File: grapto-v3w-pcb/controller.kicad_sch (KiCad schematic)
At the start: 34 parts, among them J5 Conn_01x06_Female, J6 USB_C_Receptacle_USB2.0, J7 USB_C_Receptacle_USB2.0, J8 Conn_01x06_Male, U11 USBLC6-4SC6, U12 ACN52840, U13 TPS2110, U14 LM3676SD-3.3

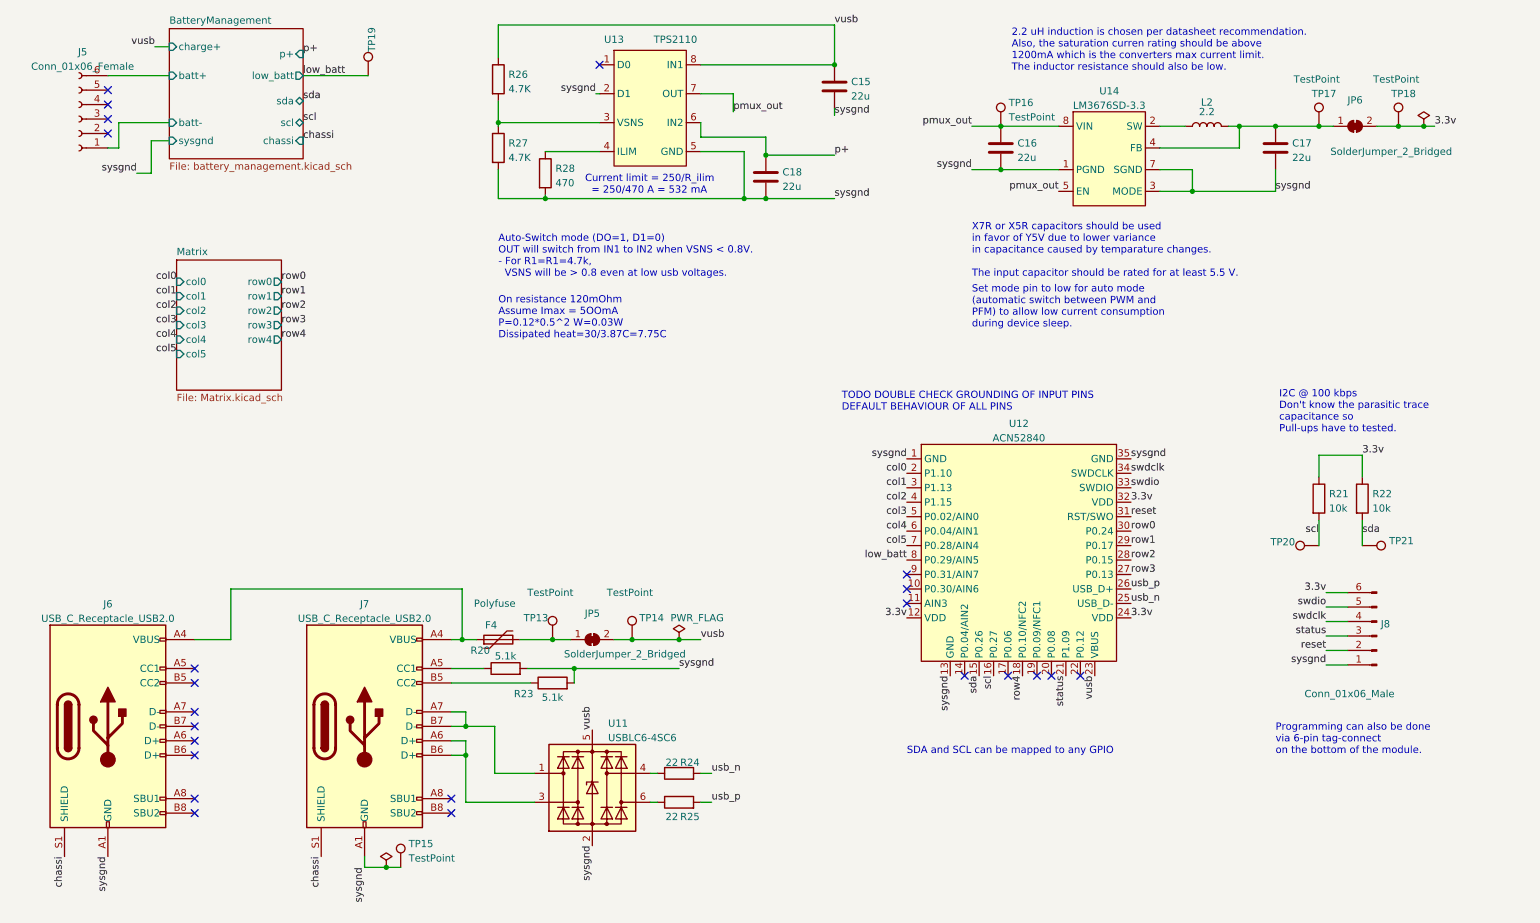
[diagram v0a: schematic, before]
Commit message: More layout. esd chip problems.
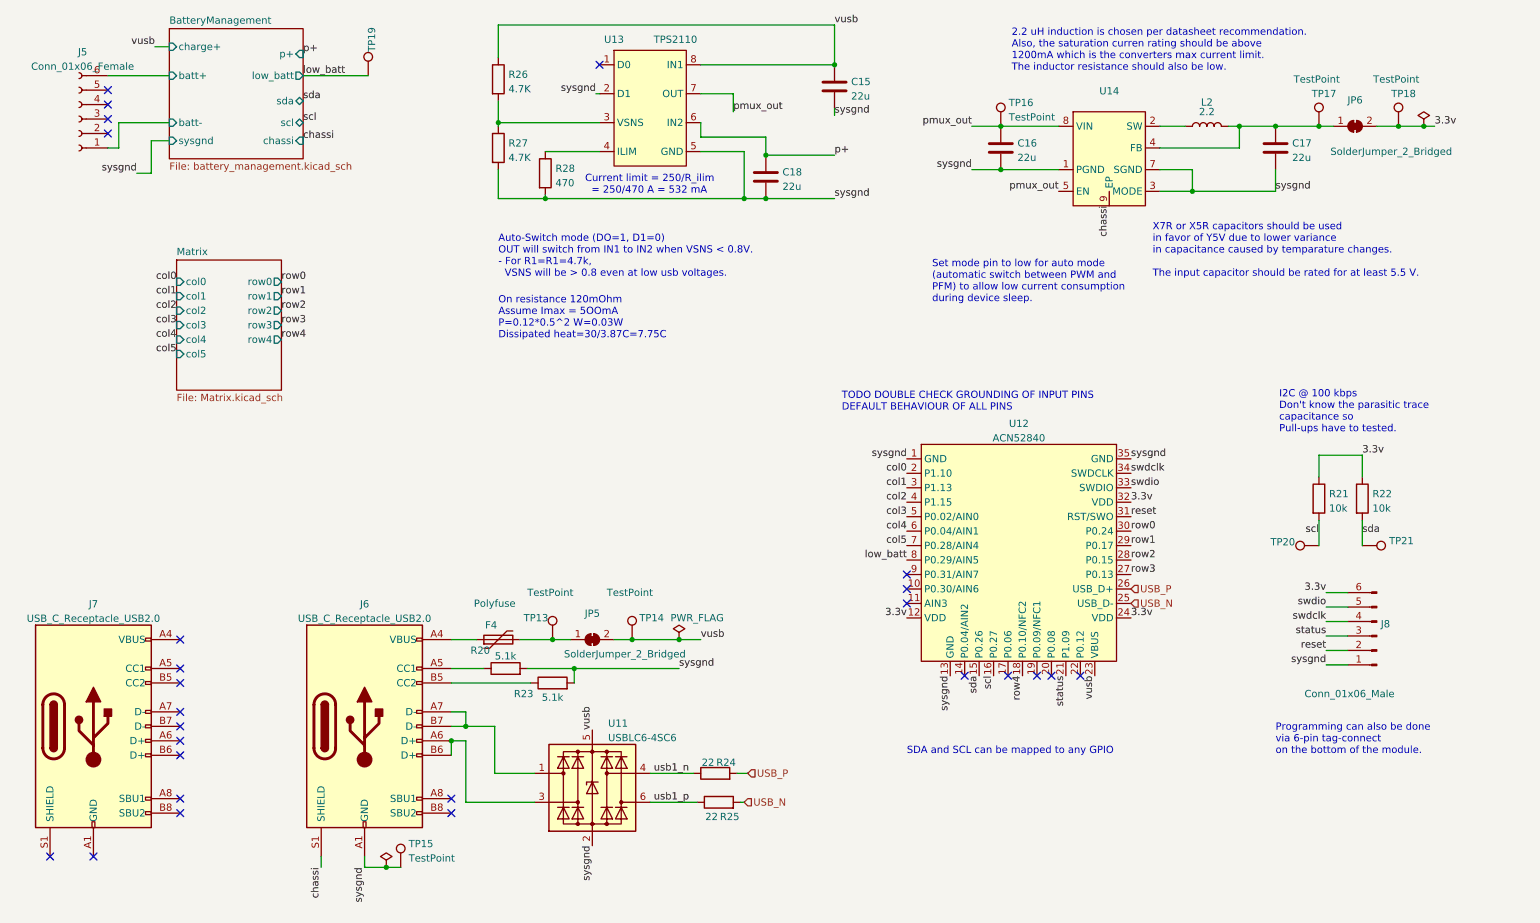
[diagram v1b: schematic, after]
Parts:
- U14: value LM3676SD-3.3 -> (none); footprint Package_SON:WSON-8-1EP_3x3mm_P0.5mm_EP1.6x2.0mm -> (none)
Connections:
- net chassi: now also U14.9 (EP); no longer J7.S1 (SHIELD)
- net sysgnd: no longer J7.A1 (GND), J7.A12 (GND), J7.B1 (GND), J7.B12 (GND)
- net at F4.1, J6.A4 (VBUS), J6.A9 (VBUS)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: no longer J7.A4 (VBUS), J7.A9 (VBUS), J7.B4 (VBUS), J7.B9 (VBUS)
- net at J6.A5 (CC1): now also R20.1
- net at J6.A6 (D+): now also J6.B6 (D+), U11.3 (I/O2)
- net at J6.A7 (D-): now also J6.B7 (D-), U11.1 (I/O1)
- net at J6.B5 (CC2): now also R23.1
- net at J7.A5 (CC1): no longer R20.1
- net at J7.B5 (CC2): no longer R23.1
- net usb1_n: now reaches R24.1, U11.4 (I/O3)
- net usb1_p: now reaches R25.1, U11.6 (I/O4)
- net usb_n renamed USB_N
- net USB_N: now also R25.2; no longer R24.2
- net usb_p renamed USB_P
- net USB_P: now also R24.2; no longer R25.2
- new net: J7.A1 (GND), J7.A12 (GND), J7.B1 (GND), J7.B12 (GND)
- new net: J7.A4 (VBUS), J7.A9 (VBUS), J7.B4 (VBUS), J7.B9 (VBUS)
- now unconnected: J7.A6 (D+), J7.A7 (D-), J7.B6 (D+), J7.B7 (D-)
- no-connect marks 23 -> 26
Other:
- moved on the sheet: J6, J7, R24, R25

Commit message: all nets connected.
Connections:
- net USB_N: now also R24.2; no longer R25.2
- net USB_P: now also R25.2; no longer R24.2
- net usb1_n: now also J6.A7 (D-), J6.B7 (D-), U11.1 (I/O1); no longer U11.4 (I/O3)
- net usb1_p: now also J6.A6 (D+), J6.B6 (D+), U11.3 (I/O2); no longer U11.6 (I/O4)
- net vusb: no longer U11.5 (VBUS)
- net VBUS_NO_FUSE: now reaches F4.1, J6.A4 (VBUS), J6.A9 (VBUS), J6.B4 (VBUS), J6.B9 (VBUS)
- net VBUS_NO_FUSE: now also U11.5 (VBUS)
- no-connect marks 26 -> 28
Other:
- moved on the sheet: U11
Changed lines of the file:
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@@
   (junction (at 120.015 142.24) (diameter 0) (color 0 0 0 0)
   )
+  (junction (at 126.365 160.655) (diameter 0) (color 0 0 0 0)
+  )
   (junction (at 130.175 137.16) (diameter 0) (color 0 0 0 0)
   )
@@
   )
   (junction (at 116.205 137.16) (diameter 0) (color 0 0 0 0)
+  )
+  (junction (at 121.285 165.735) (diameter 0) (color 0 0 0 0)
   )
   (junction (at 165.735 36.195) (diameter 0) (color 0 0 0 0)
@@
   (no_connect (at 38.1 45.72))
   (no_connect (at 38.1 40.64))
+  (no_connect (at 126.365 189.23))
+  (no_connect (at 121.285 189.23))
   (no_connect (at 98.425 167.64))
   (no_connect (at 98.425 165.1))
@@
     (stroke (width 0) (type default) (color 0 0 0 0))
   )
+  (wire (pts (xy 121.285 165.735) (xy 141.605 165.735))
+    (stroke (width 0) (type default) (color 0 0 0 0))
+  )
   (wire (pts (xy 165.735 29.21) (xy 106.68 29.21))
     (stroke (width 0) (type default) (color 0 0 0 0))
   )
-  (wire (pts (xy 133.35 160.655) (xy 140.97 160.655))
-    (stroke (width 0) (type default) (color 0 0 0 0))
-  )
-  (wire (pts (xy 113.03 165.735) (xy 100.965 165.735))
-    (stroke (width 0) (type default) (color 0 0 0 0))
-  )
-  (wire (pts (xy 113.03 160.655) (xy 106.045 160.655))
+  (wire (pts (xy 106.045 160.655) (xy 126.365 160.655))
     (stroke (width 0) (type default) (color 0 0 0 0))
   )
@@
     (stroke (width 0) (type default) (color 0 0 0 0))
   )
+  (wire (pts (xy 126.365 160.655) (xy 140.97 160.655))
+    (stroke (width 0) (type default) (color 0 0 0 0))
+  )
   (wire (pts (xy 110.49 137.16) (xy 116.205 137.16))
     (stroke (width 0) (type default) (color 0 0 0 0))
@@
     (stroke (width 0) (type default) (color 0 0 0 0))
   )
-  (wire (pts (xy 149.225 165.735) (xy 149.86 165.735))
+  (wire (pts (xy 149.225 165.735) (xy 156.845 165.735))
+    (stroke (width 0) (type default) (color 0 0 0 0))
+  )
+  (wire (pts (xy 121.285 165.735) (xy 121.285 168.91))
     (stroke (width 0) (type default) (color 0 0 0 0))
   )
@@
     (stroke (width 0) (type default) (color 0 0 0 0))
   )
-  (wire (pts (xy 133.35 165.735) (xy 141.605 165.735))
+  (wire (pts (xy 100.965 165.735) (xy 121.285 165.735))
     (stroke (width 0) (type default) (color 0 0 0 0))
   )
@@
   )
   (wire (pts (xy 258.445 116.205) (xy 258.445 120.65))
+    (stroke (width 0) (type default) (color 0 0 0 0))
+  )
+  (wire (pts (xy 126.365 160.655) (xy 126.365 168.91))
     (stroke (width 0) (type default) (color 0 0 0 0))
   )
@@
     (effects (font (size 1.27 1.27)) (justify left bottom))
   )
-  (label "sysgnd" (at 123.19 173.355 270)
+  (label "sysgnd" (at 113.665 179.07 180)
     (effects (font (size 1.27 1.27)) (justify right bottom))
   )
@@
     (effects (font (size 1.27 1.27)) (justify right bottom))
   )
+  (label "VBUS_NO_FUSE" (at 100.965 137.16 90)
+    (effects (font (size 1.27 1.27)) (justify left bottom))
+  )
   (label "swdio" (at 252.095 131.445 180)
     (effects (font (size 1.27 1.27)) (justify right bottom))
@@
     (effects (font (size 1.27 1.27)) (justify right bottom))
   )
-  (label "vusb" (at 123.19 153.035 90)
-    (effects (font (size 1.27 1.27)) (justify left bottom))
-  )
   (label "col5" (at 50.165 86.995 180)
     (effects (font (size 1.27 1.27)) (justify right bottom))
@@
   )
   (label "usb1_p" (at 133.985 165.735 0)
+    (effects (font (size 1.27 1.27)) (justify left bottom))
+  )
+  (label "VBUS_NO_FUSE" (at 133.985 179.07 0)
     (effects (font (size 1.27 1.27)) (justify left bottom))
   )
@@
     (effects (font (size 1.27 1.27)) (justify left))
   )
-  (hierarchical_label "USB_P" (shape input) (at 150.495 160.655 0)
+  (hierarchical_label "USB_P" (shape input) (at 156.845 165.735 0)
     (effects (font (size 1.27 1.27)) (justify left))
   )
@@
     (effects (font (size 1.27 1.27)) (justify left))
   )
-  (hierarchical_label "USB_N" (shape input) (at 149.86 165.735 0)
+  (hierarchical_label "USB_N" (shape input) (at 150.495 160.655 0)
     (effects (font (size 1.27 1.27)) (justify left))
   )
@@
     (pin "2")
   )
-  (symbol (lib_id "Power_Protection:USBLC6-4SC6") (at 123.19 163.195 0) (unit 1)
-    (in_bom yes) (on_board yes) (fields_autoplaced)
-    (property "Reference" "U11" (id 0) (at 125.9587 151.8752 0)
-      (effects (font (size 1.27 1.27)) (justify left))
-    )
-    (property "Value" "USBLC6-4SC6" (id 1) (at 125.9587 154.4121 0)
-      (effects (font (size 1.27 1.27)) (justify left))
-    )
-    (property "Footprint" "Package_TO_SOT_SMD:SOT-23-6" (id 2) (at 123.19 175.895 0)
-      (effects (font (size 1.27 1.27)) hide)
-    )
-    (property "Datasheet" "https://www.st.com/resource/en/datasheet/usblc6-4.pdf" (id 3) (at 128.27 154.305 0)
-      (effects (font (size 1.27 1.27)) hide)
-    )
+  (symbol (lib_id "Power_Protection:USBLC6-4SC6") (at 123.825 179.07 270) (unit 1)
+    (in_bom yes) (on_board yes)
+    (property "Reference" "U11" (id 0) (at 139.1807 174.4811 90))
+    (property "Value" "USBLC6-4SC6" (id 1) (at 140.335 183.515 90))
+    (property "Footprint" "Package_TO_SOT_SMD:SOT-23-6" (id 2) (at 111.125 179.07 0)
+      (effects (font (size 1.27 1.27)) hide)
+    )
+    (property "Datasheet" "https://www.st.com/resource/en/datasheet/usblc6-4.pdf" (id 3) (at 132.715 184.15 0)
+      (effects (font (size 1.27 1.27)) hide)
+    )

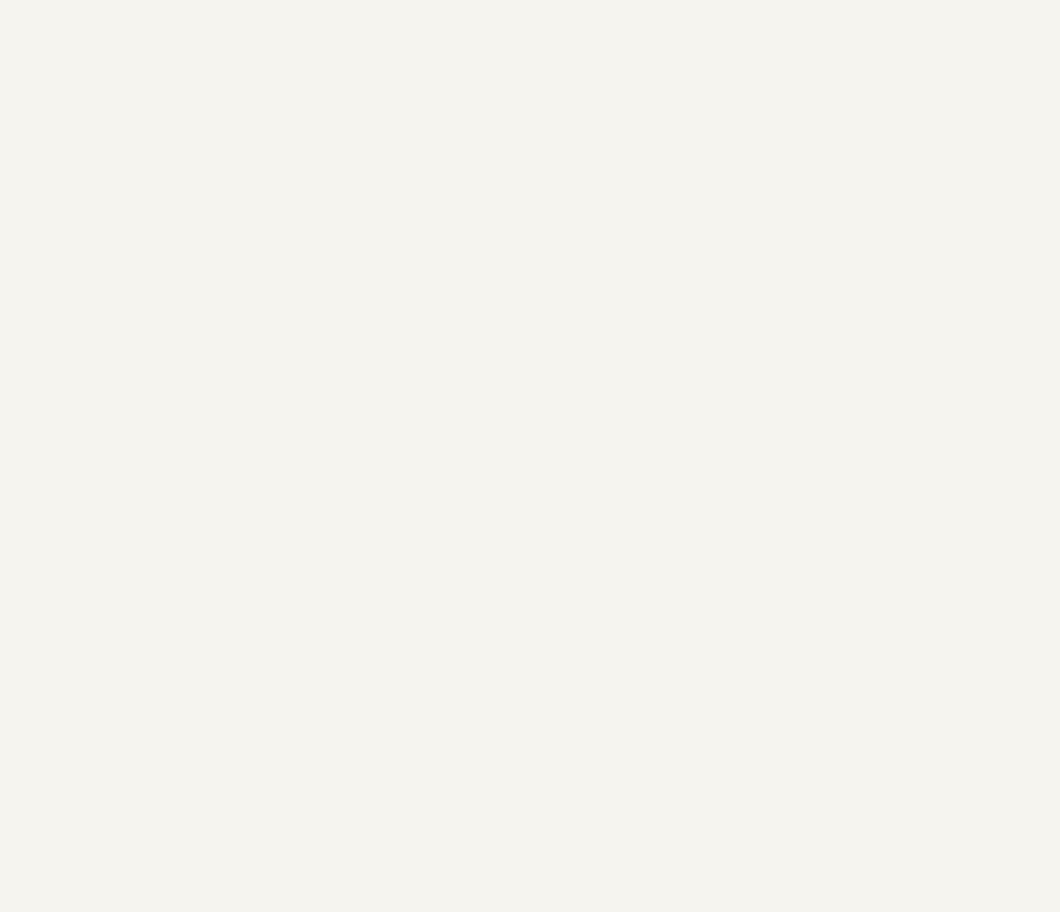
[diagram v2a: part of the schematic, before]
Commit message: Began changing mcu module.
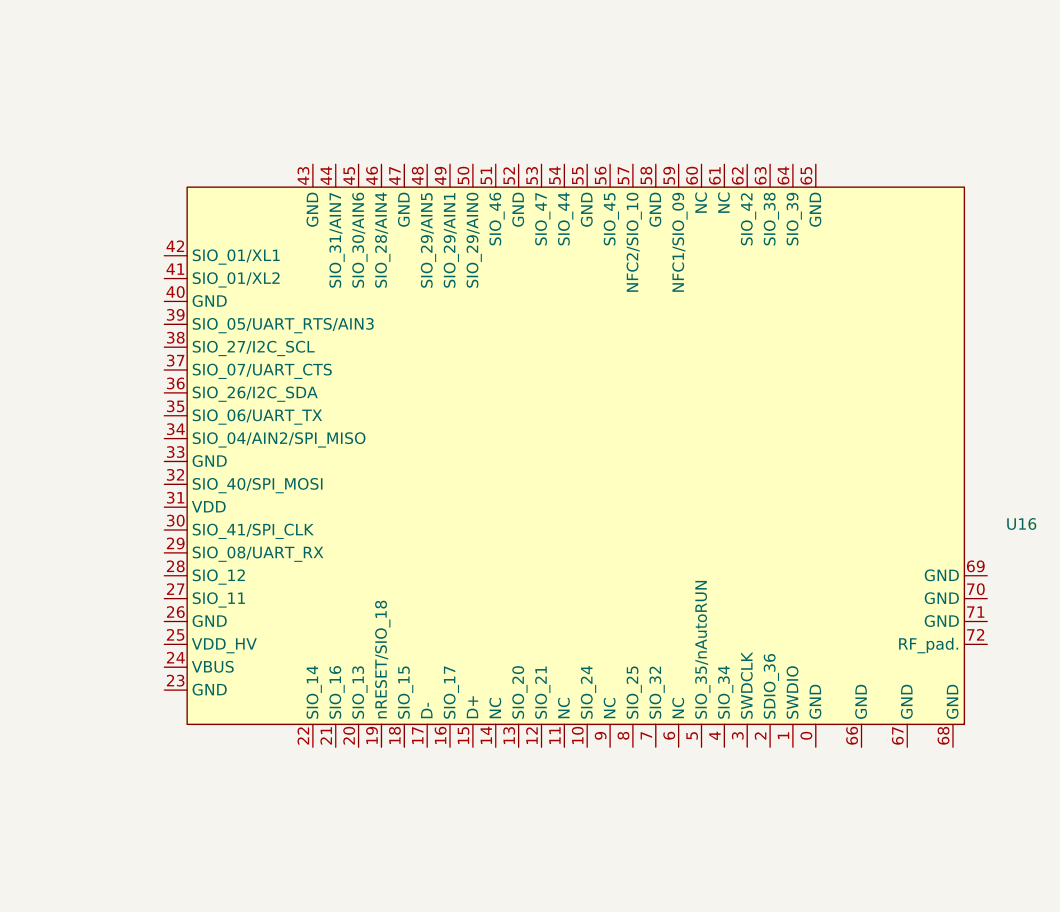
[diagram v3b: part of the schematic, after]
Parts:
- added U16: (no value), symbol grapto-v3w:Laird_bl653
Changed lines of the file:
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@@
     (pin "2")
+  )
+  (symbol (lib_id "grapto-v3w:Laird_bl653") (at 346.075 121.92 0) (unit 1)
+    (in_bom yes) (on_board yes) (fields_autoplaced)
+    (property "Reference" "U16" (id 0) (at 398.1494 125.1035 0))
+    (property "Value" "" (id 1) (at 398.1494 127.6404 0))
+    (property "Footprint" "" (id 2) (at 362.585 124.46 0)
+      (effects (font (size 1.27 1.27)) hide)
+    )
+    (property "Datasheet" "" (id 3) (at 362.585 124.46 0)
+      (effects (font (size 1.27 1.27)) hide)
+    )
+    (pin "0")
+    (pin "1")
+    (pin "10")
+    (pin "11")
+    (pin "12")
+    (pin "13")
+    (pin "14")
+    (pin "15")
+    (pin "16")
+    (pin "17")
+    (pin "18")
+    (pin "19")
+    (pin "2")
+    (pin "20")
+    (pin "21")
+    (pin "22")
+    (pin "23")
+    (pin "24")
+    (pin "25")
+    (pin "26")
+    (pin "27")
+    (pin "28")
+    (pin "29")
+    (pin "3")
+    (pin "30")
+    (pin "31")
+    (pin "32")
+    (pin "33")
+    (pin "34")
+    (pin "35")
+    (pin "36")
+    (pin "37")
+    (pin "38")
+    (pin "39")
+    (pin "4")
+    (pin "40")
+    (pin "41")
+    (pin "42")
+    (pin "43")
+    (pin "44")
+    (pin "45")
+    (pin "46")
+    (pin "47")
+    (pin "48")
+    (pin "49")
+    (pin "5")
+    (pin "50")
+    (pin "51")
+    (pin "52")
+    (pin "53")
+    (pin "54")
+    (pin "55")
+    (pin "56")
+    (pin "57")
+    (pin "58")
+    (pin "59")
+    (pin "6")
+    (pin "60")
+    (pin "61")
+    (pin "62")
+    (pin "63")
+    (pin "64")
+    (pin "65")
+    (pin "66")
+    (pin "67")
+    (pin "68")
+    (pin "69")
+    (pin "7")
+    (pin "70")
+    (pin "71")
+    (pin "72")
+    (pin "8")
+    (pin "9")
   )
   (symbol (lib_id "grapto-v3w:TPS2110") (at 133.35 43.815 0) (unit 1)

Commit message: Removing fuel gauge. Going for 2-layer board.
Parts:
- removed R21, R22: 10k, Resistor_SMD:R_0603_1608Metric_Pad0.98x0.95mm_HandSolder, symbol Device:R
- removed TP20, TP21: (no value), symbol Connector:TestPoint
- removed U12: ACN52840, symbol grapto-v3w:ACN52840
- TP13, TP14, TP15, TP16, TP17, TP18: footprint (none) -> TestPoint:TestPoint_THTPad_D2.0mm_Drill1.0mm
- TP22: renamed from TP19; footprint (none) -> TestPoint:TestPoint_THTPad_D2.0mm_Drill1.0mm
- U14: value (none) -> LM3676SD-3.3; footprint (none) -> Package_SON:WSON-8-1EP_3x3mm_P0.5mm_EP1.6x2.0mm
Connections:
- net 3.3v: now also U16.25 (VDD_HV), U16.31 (VDD)
- net USB_N: now also U16.17 (D-)
- net USB_P: now also U16.15 (D+)
- net col0: now also U16.4 (SIO_34)
- net col1: now also U16.5 (SIO_35/nAutoRUN)
- net col2: now also U16.7 (SIO_32)
- net col3: now also U16.8 (SIO_25)
- net col4: now also U16.10 (SIO_24)
- net col5: now also U16.12 (SIO_21)
- net low_batt: now also U16.45 (SIO_30/AIN6)
- net row0: now also U16.46 (SIO_28/AIN4)
- net row1: now also U16.48 (SIO_29/AIN5)
- net row2: now also U16.49 (SIO_03/AIN1)
- net row3: now also U16.50 (SIO_02/AIN0)
- net row4: now also U16.51 (SIO_46)
- net status: now also U16.13 (SIO_20)
- net swdclk: now also U16.3 (SWDCLK)
- net swdio: now also U16.1 (SWDIO)
- net sysgnd: now also U16.0 (GND), U16.23 (GND), U16.26 (GND), U16.33 (GND), U16.40 (GND), U16.43 (GND), U16.47 (GND), U16.52 (GND), U16.55 (GND), U16.58 (GND), U16.65 (GND), U16.66 (GND), U16.67 (GND), U16.68 (GND), U16.69 (GND), U16.70 (GND), U16.71 (GND)
- net vusb: now also U16.24 (VBUS)
- no-connect marks 28 -> 56
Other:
- sheet BatteryManagement ports: added none; removed chassi, scl, sda
- note removed: "I2C @ 100 kbps Don't know the parasitic trace capacitance so Pull-ups have to tested."
- note removed: "SDA and SCL can be mapped to any GPIO"
- note removed: "TODO DOUBLE CHECK GROUNDING OF INPUT PINS DEFAULT BEHAVIOUR OF ALL PINS"
- moved on the sheet: J5, J8, TP22, U16
